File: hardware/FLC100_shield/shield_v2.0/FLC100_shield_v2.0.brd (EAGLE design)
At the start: 99.1 x 78.7 mm, 73 parts, among them IC1 TSR 1-2450, IC4 MCP1640SOT23-6-HAND, J1 RJ11-6PTH, Q1 2N7000, Q2 2N7000, Q3 2N7000, Q4 2N7000, Q5 2N7000, Q6 2N7000, Q7 2N7000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

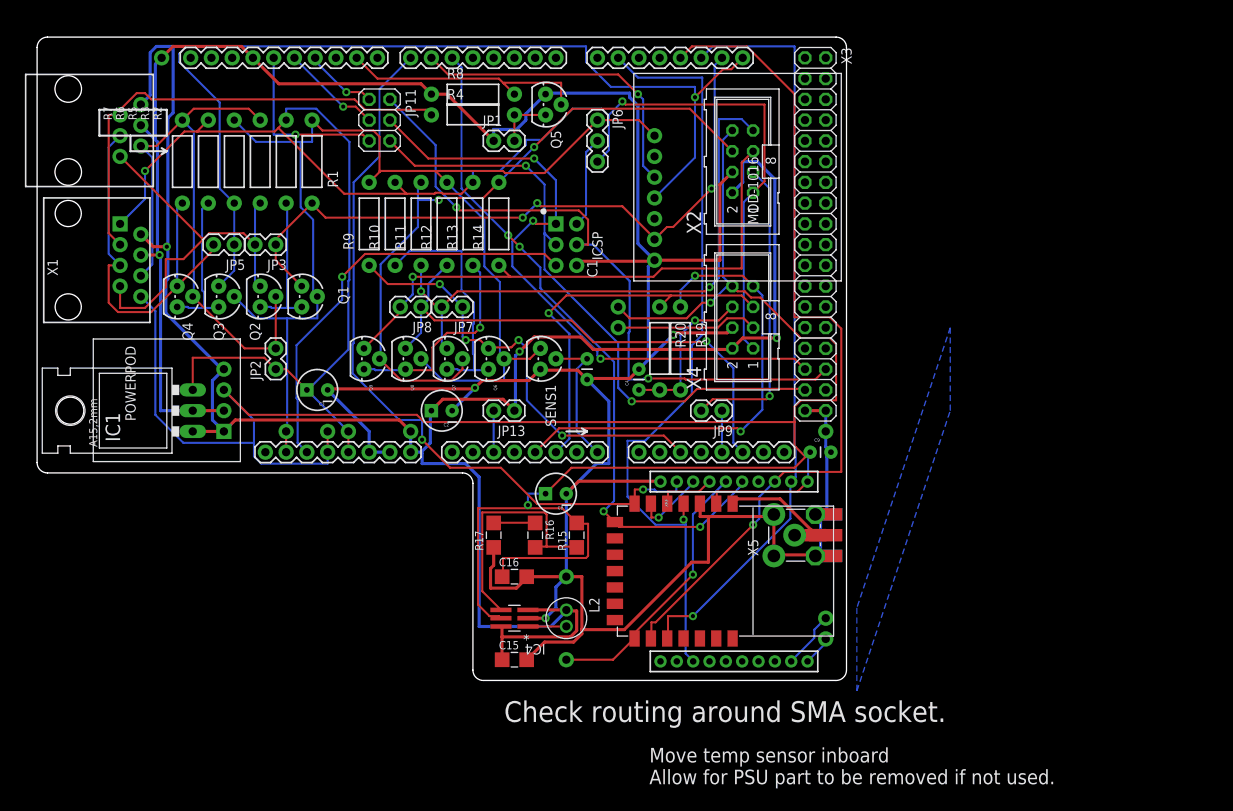
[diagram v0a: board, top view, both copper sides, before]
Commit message: Simplifying circuit.
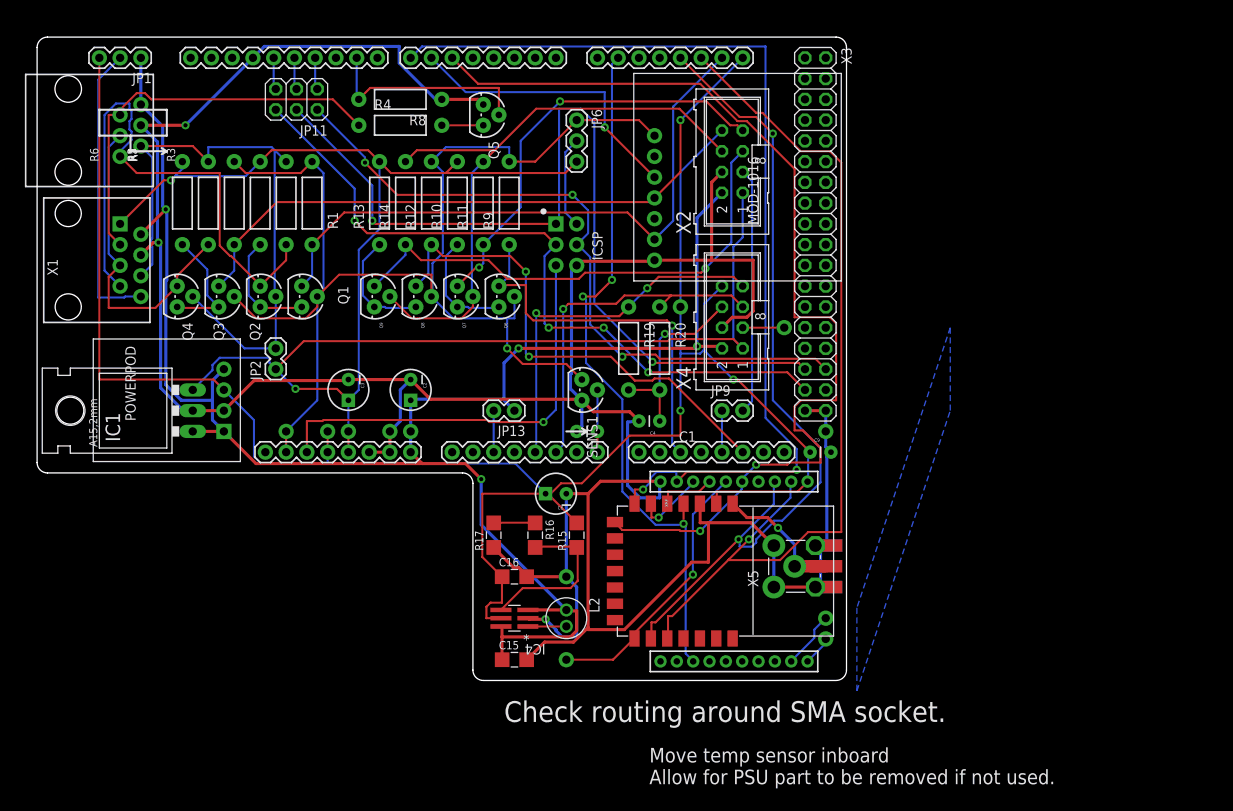
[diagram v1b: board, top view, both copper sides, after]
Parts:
- removed JP3: MAG SDA, SparkFun:1X02
- removed JP5: MAG SCL, SparkFun:1X02
- removed JP7: CLOUD SDA, SparkFun:1X02
- removed JP8: CLOUD SCL, SparkFun:1X02
- JP1: value SHDN -> ISP VCC; device SparkFun:1X02 -> SparkFun:1X03
- moved U$16 53.6 mm to (43.2, 30.5)
- moved JP1 44.4 mm to (12.7, 76.2), turned to 180 degrees
- moved U$5 20.3 mm to (91.4, 43.2)
- moved R9 17.3 mm to (57.8, 58.4)
- moved R13 11.7 mm to (41.9, 58.4)
- moved R14 11.7 mm to (45.1, 58.4)
- moved JP11 10.5 mm to (31.8, 71.1), turned to 180 degrees
- moved R4 8.98 mm to (44.5, 67.9)
- moved C1 8.98 mm to (68.6, 30.5), turned to 180 degrees
- moved R8 8.91 mm to (44.5, 71.1), turned to 180 degrees
- moved R10 8.03 mm to (51.4, 58.4)
- moved R11 8.03 mm to (54.6, 58.4)
- moved Q6 7.73 mm to (56.5, 47.0)
- moved Q7 7.73 mm to (51.4, 47.0)
- moved Q8 7.73 mm to (46.4, 47.0)
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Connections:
- new net N$7: JP1.2, X1.8
- net +3V3: now also JP1.3; no longer X1.8
- net 16: no longer JP7.1
- net 19: no longer JP8.1
- net CLOUD_SCL: no longer JP8.2
- net CLOUD_SDA: no longer JP7.2
- net GND: no longer JP1.1
- net MAG_SCL: no longer JP5.2
- net MAG_SDA: no longer JP3.2
- net SCL: no longer JP5.1
- net SDA: no longer JP3.1
- net SHDN: no longer JP1.2
- net VIN: now also JP1.1
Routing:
- net +3V3: track 296.7 -> 244.8 mm
- net SCL: track 122.2 -> 81.3 mm
- net !XRF_RESET: track 84.5 -> 124.5 mm, vias 4 -> 2
- net N$7: track 0.00 -> 35.7 mm
- net MISO: track 79.6 -> 110.6 mm, vias 3 -> 2
- net VIN: track 244.9 -> 214.9 mm, vias 3 -> 4
- net XRF_SLEEP: track 92.3 -> 121.9 mm
- net CLOUD_SDA: track 71.5 -> 51.9 mm
- net MAG_SDA: track 50.6 -> 68.1 mm
- net 13: track 21.4 -> 3.92 mm, vias 1 -> 0
- net GND: track 409.4 -> 393.1 mm, vias 4 -> 3
- net RX1: track 92.8 -> 108.7 mm
- net N$4: track 29.5 -> 14.0 mm
- net HUMIDITY_SDA: track 58.1 -> 45.0 mm
- net SCK: track 75.9 -> 88.9 mm, vias 2 -> 4
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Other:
- board text added: "Add silkscreen lines to indicate where to link when I2C level shifting not required."
- board text added: "Check jumpers are easily fitted and other components are out of the way"

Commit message: Tidying silkscreen.
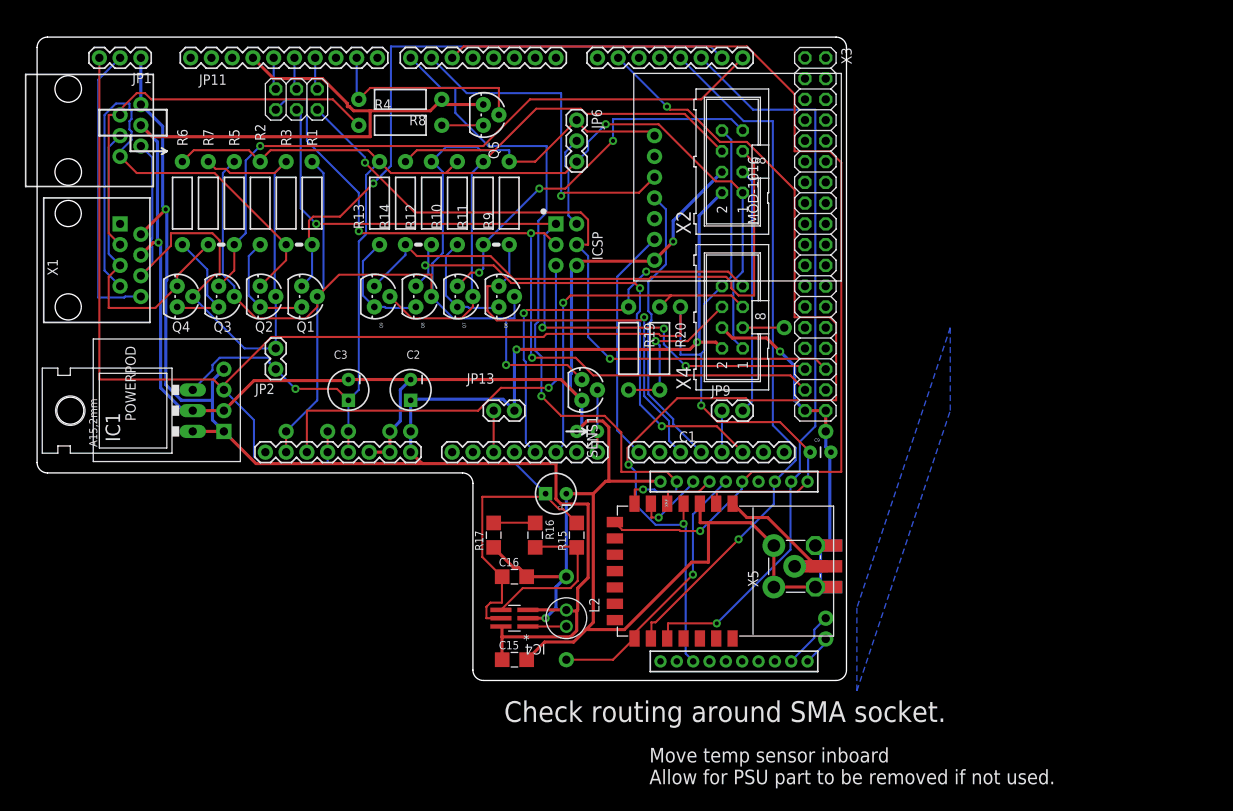
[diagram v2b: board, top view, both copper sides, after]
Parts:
- removed C4: 100n, SparkFun:CAP-PTH-SMALL
- R8: value 100k -> 1M
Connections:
- new net 14: MOD-1016.SDA_MOSI, U$13.14
- new net 17: MOD-1016.SCL, U$13.17
- net +5V: no longer X1.1
- net GND: no longer C4.2
- net N$22: no longer C4.1
- net SCL: no longer MOD-1016.SCL
- net SDA: no longer MOD-1016.SDA_MOSI
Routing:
- net +5V: track 205.3 -> 160.7 mm
- net XRF_SLEEP: track 121.9 -> 86.3 mm
- net 17: track 0.00 -> 35.6 mm
- net XRF_ON: track 86.9 -> 121.1 mm
- net +3V3: track 244.8 -> 278.7 mm, vias 2 -> 1
- net 14: track 0.00 -> 29.0 mm
- net MISO: track 110.6 -> 93.0 mm, vias 2 -> 4
- net RX1: track 108.7 -> 92.3 mm
- net TX1: track 100.5 -> 86.6 mm, vias 2 -> 1
- net VIN: track 214.9 -> 225.9 mm, vias 4 -> 3
- net MAG_VCC: track 75.3 -> 85.8 mm
- net SCK: track 88.9 -> 98.2 mm, vias 4 -> 3
- net CLOUD_SCL: track 61.9 -> 70.9 mm, vias 1 -> 0
- net GND: track 393.1 -> 384.9 mm, vias 3 -> 4
- net IOREF: track 158.4 -> 166.6 mm
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
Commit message: Development of new FLC100 shield.
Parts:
- added C4: 100n, SparkFun:CAP-PTH-SMALL
- moved R1 1.27 mm to (33.7, 57.1)
- moved R10 1.27 mm to (51.4, 57.1)
- moved R11 1.27 mm to (54.6, 57.1)
- moved R12 1.27 mm to (48.3, 57.1)
- moved R13 1.27 mm to (41.9, 57.1)
- moved R14 1.27 mm to (45.1, 57.1)
- moved R2 1.27 mm to (27.3, 57.1)
- moved R3 1.27 mm to (30.5, 57.1)
- moved R5 1.27 mm to (24.1, 57.1)
- moved R6 1.27 mm to (17.8, 57.1)
- moved R7 1.27 mm to (21.0, 57.1)
- moved R9 1.27 mm to (57.8, 57.1)
- turned R19 to 90 degrees
- turned R20 to 90 degrees
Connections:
- net +5V: no longer X4.1
- net GND: now also C4.2
- net IOREF: now also X4.1
- net N$22: now also C4.1
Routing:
- net GND: track 384.9 -> 5.08 mm, vias 4 -> 0
- net +3V3: track 278.7 -> 34.9 mm
- net VIN: track 225.9 -> 0.00 mm, vias 3 -> 0
- net IOREF: track 166.6 -> 0.00 mm, vias 1 -> 0
- net +5V: track 160.7 -> 0.00 mm, vias 2 -> 0
- net !XRF_RESET: track 127.7 -> 0.00 mm, vias 1 -> 0
- net XRF_ON: track 121.1 -> 0.00 mm, vias 3 -> 0
- net SCK: track 98.2 -> 0.00 mm, vias 3 -> 0
- net MISO: track 93.0 -> 0.00 mm, vias 4 -> 0
- net RX1: track 92.3 -> 0.00 mm, vias 1 -> 0
- net TX1: track 86.6 -> 0.00 mm, vias 1 -> 0
- net XRF_SLEEP: track 86.3 -> 0.00 mm, vias 2 -> 0
- net MOSI: track 86.1 -> 0.00 mm, vias 2 -> 0
- net MAG_VCC: track 85.8 -> 0.00 mm
- net SCL: track 82.8 -> 0.00 mm, vias 1 -> 0
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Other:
- board text added: "ISP"
- board text removed: "ICSP"

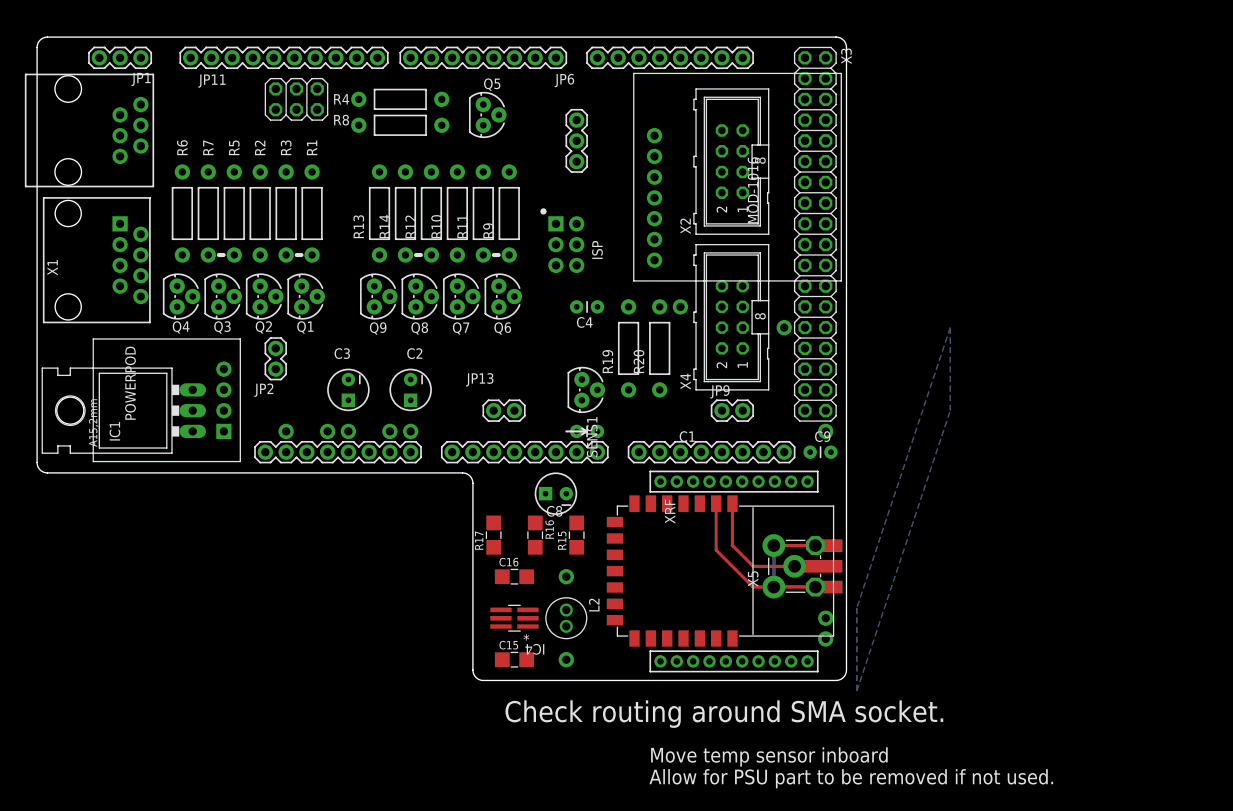
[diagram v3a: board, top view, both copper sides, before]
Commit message: Removed SRF, layout changes. Routing and silkscreen tidying.
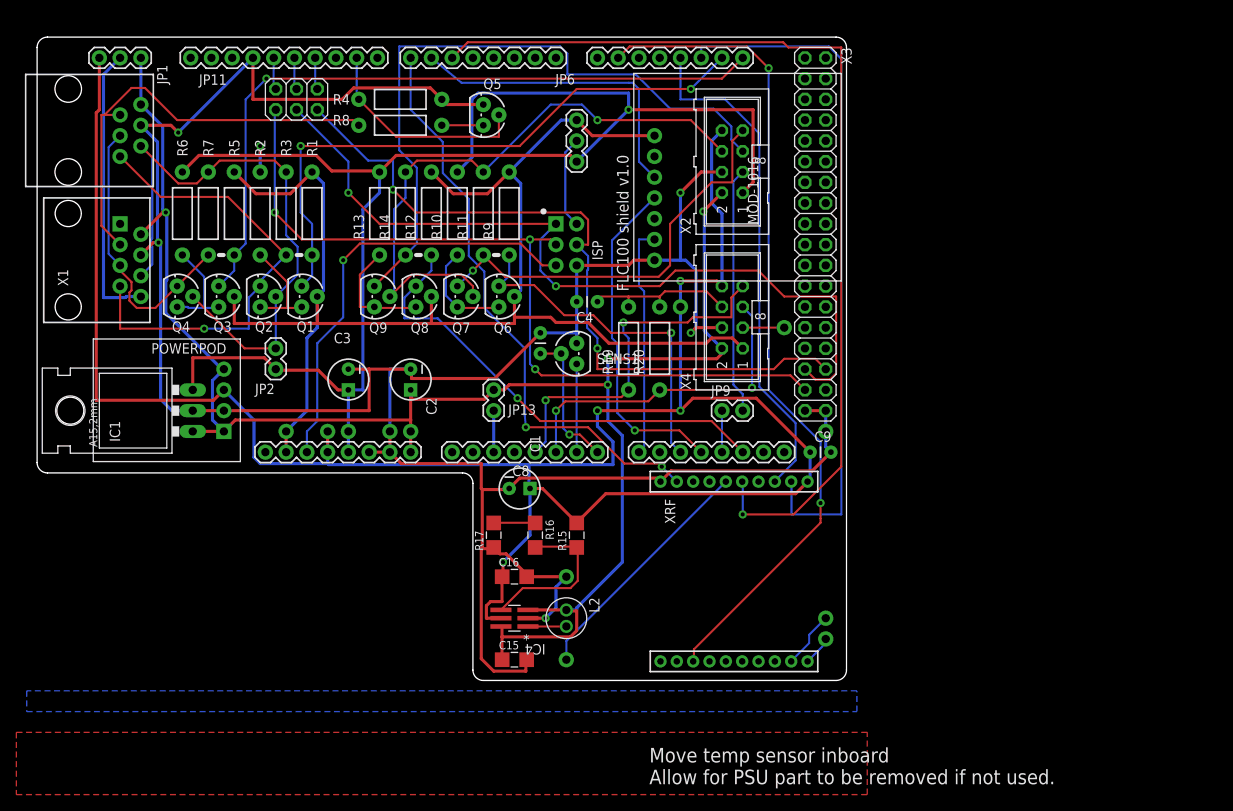
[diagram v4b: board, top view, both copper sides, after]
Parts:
- removed SRF: (no value), Ciseco Footprints:SRF-LANDING
- removed X5: SMA, SteveMarple:SMA-THD-EDGE
- JP1: value ISP VCC -> MAG VCC
- moved C1 11.8 mm to (61.6, 40.0), turned to 90 degrees
- moved C8 4.49 mm to (59.1, 23.5), turned to 0 degrees
- moved SENS1 4.49 mm to (66.0, 40.0), turned to 90 degrees
- moved JP13 3.59 mm to (55.9, 35.6), turned to 270 degrees
- moved C2 1.27 mm to (45.7, 36.8)
- moved C3 1.27 mm to (38.1, 36.8)
- moved C4 0.63 mm to (68.6, 46.4)
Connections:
- removed net ANTENNA: SRF.8, X5.SIG, X5.SIG@EDGE
- new net A6: SENS1.1, U$13.A6
- net !XRF_RESET: no longer SRF.15
- net +3V3: no longer SRF.9
- net GND: no longer SRF.10, X5.GND@0, X5.GND@1, X5.GND@2, X5.GND@3, X5.GND@EDGE0, X5.GND@EDGE1, X5.GND@EDGE2, X5.GND@EDGE3
- net IOREF: no longer SENS1.1
- net RX1: no longer SRF.3
- net TX1: no longer SRF.2
- net XRF_HEARTBEAT: no longer SRF.1
- net XRF_ON: no longer SRF.11
- net XRF_P1_5: no longer SRF.13
- net XRF_P1_6: no longer SRF.12
- net XRF_SLEEP: no longer SRF.14
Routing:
- net GND: track 5.08 -> 335.6 mm, vias 0 -> 5
- net +3V3: track 34.9 -> 259.6 mm, vias 1 -> 4
- net VIN: track 0.00 -> 209.2 mm, vias 0 -> 4
- net +5V: track 0.00 -> 183.0 mm, vias 0 -> 2
- net IOREF: track 0.00 -> 175.1 mm
- net !XRF_RESET: track 0.00 -> 118.5 mm, vias 0 -> 1
- net XRF_ON: track 0.00 -> 101.8 mm, vias 0 -> 2
- net MISO: track 0.00 -> 99.4 mm, vias 0 -> 2
- net SCK: track 0.00 -> 98.9 mm, vias 0 -> 3
- net MOSI: track 0.00 -> 90.6 mm, vias 0 -> 2
- net SCL: track 0.00 -> 87.2 mm, vias 0 -> 1
- net RX1: track 0.00 -> 85.0 mm
- net CLOUD_SCL: track 0.00 -> 82.2 mm
- net CLOUD_VCC: track 0.00 -> 74.8 mm, vias 0 -> 1
- net MAG_VCC: track 0.00 -> 74.6 mm
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- added copper zone on layer 1, net GND
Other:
- board text added: "+3V3"
- board text added: "+5V"
- board text added: "IOREF"
- board text added: "VIN"
- board text removed: "Check routing around SMA socket."

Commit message: Minor adjustments for PCB layout.
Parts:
- removed U$15: PAD, SteveMarple:PAD
- added U$2, U$4: PAD, SteveMarple:PAD
- C3: value 4u7 25V -> 4u7
- IC4: value MCP1640SOT23-6-HAND -> MCP1640
- moved R3 2.54 mm to (33.0, 57.1)
- moved R5 2.54 mm to (26.7, 57.1)
- moved R7 2.54 mm to (23.5, 57.1)
- moved Q1 2.54 mm to (34.9, 47.0)
- moved Q2 2.54 mm to (29.8, 47.0)
- moved Q3 2.54 mm to (24.8, 47.0)
- moved Q4 2.54 mm to (19.7, 47.0)
- moved R1 2.54 mm to (36.2, 57.1)
- moved R2 2.54 mm to (29.8, 57.1)
- moved R6 2.54 mm to (20.3, 57.1)
- moved C16 1.27 mm to (59.7, 12.7)
- moved U$32 1.27 mm to (63.5, 2.54)
- moved U$40 1.27 mm to (63.5, 12.7)
- moved C9 0.64 mm to (94.6, 27.3), turned to 90 degrees
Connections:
- net GND: no longer U$15.1
- net XRF_P1_5: now also U$4.1
- net XRF_P1_6: now also U$2.1
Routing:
- net MAG_SCL: track 34.7 -> 47.3 mm
- net +3V3: track 259.6 -> 271.0 mm
- net GND: track 335.6 -> 346.0 mm
- net MAG_SDA: track 57.2 -> 62.3 mm
- net XRF_HEARTBEAT: track 29.9 -> 34.2 mm
- net XRF_P1_5: track 0.00 -> 4.18 mm
- net XRF_P1_6: track 0.00 -> 4.15 mm
- net MAG_VCC: track 74.6 -> 78.4 mm
- net +5V: track 183.0 -> 186.6 mm
- net XRF_ON: track 101.8 -> 105.1 mm
- net ISP_VCC: track 11.3 -> 13.8 mm
- net SDA: track 74.3 -> 71.9 mm
- net N$7: track 34.8 -> 36.6 mm
- net IOREF: track 175.1 -> 173.6 mm
- net SCK: track 98.9 -> 100.1 mm
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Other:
- board text removed: "Add silkscreen lines to indicate where to link when I2C level shifting not required."
- board text removed: "Check jumpers are easily fitted and other components are out of the way"
- board text removed: "Move temp sensor inboard Allow for PSU part to be removed if not used."
